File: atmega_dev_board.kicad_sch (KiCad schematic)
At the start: 44 parts, among them J1 1x15 Pin Header, J2 USB_C_Receptacle_USB2.0_16P, J3 1x15 Pin Header, J4 2x3 Pin Header, SW1 Push Button, SW2 Push Button, U1 78L05G-AB3-R, U2 HT7533-1, U3 ATmega328P-A, U4 CP2102N-Axx-xQFN28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

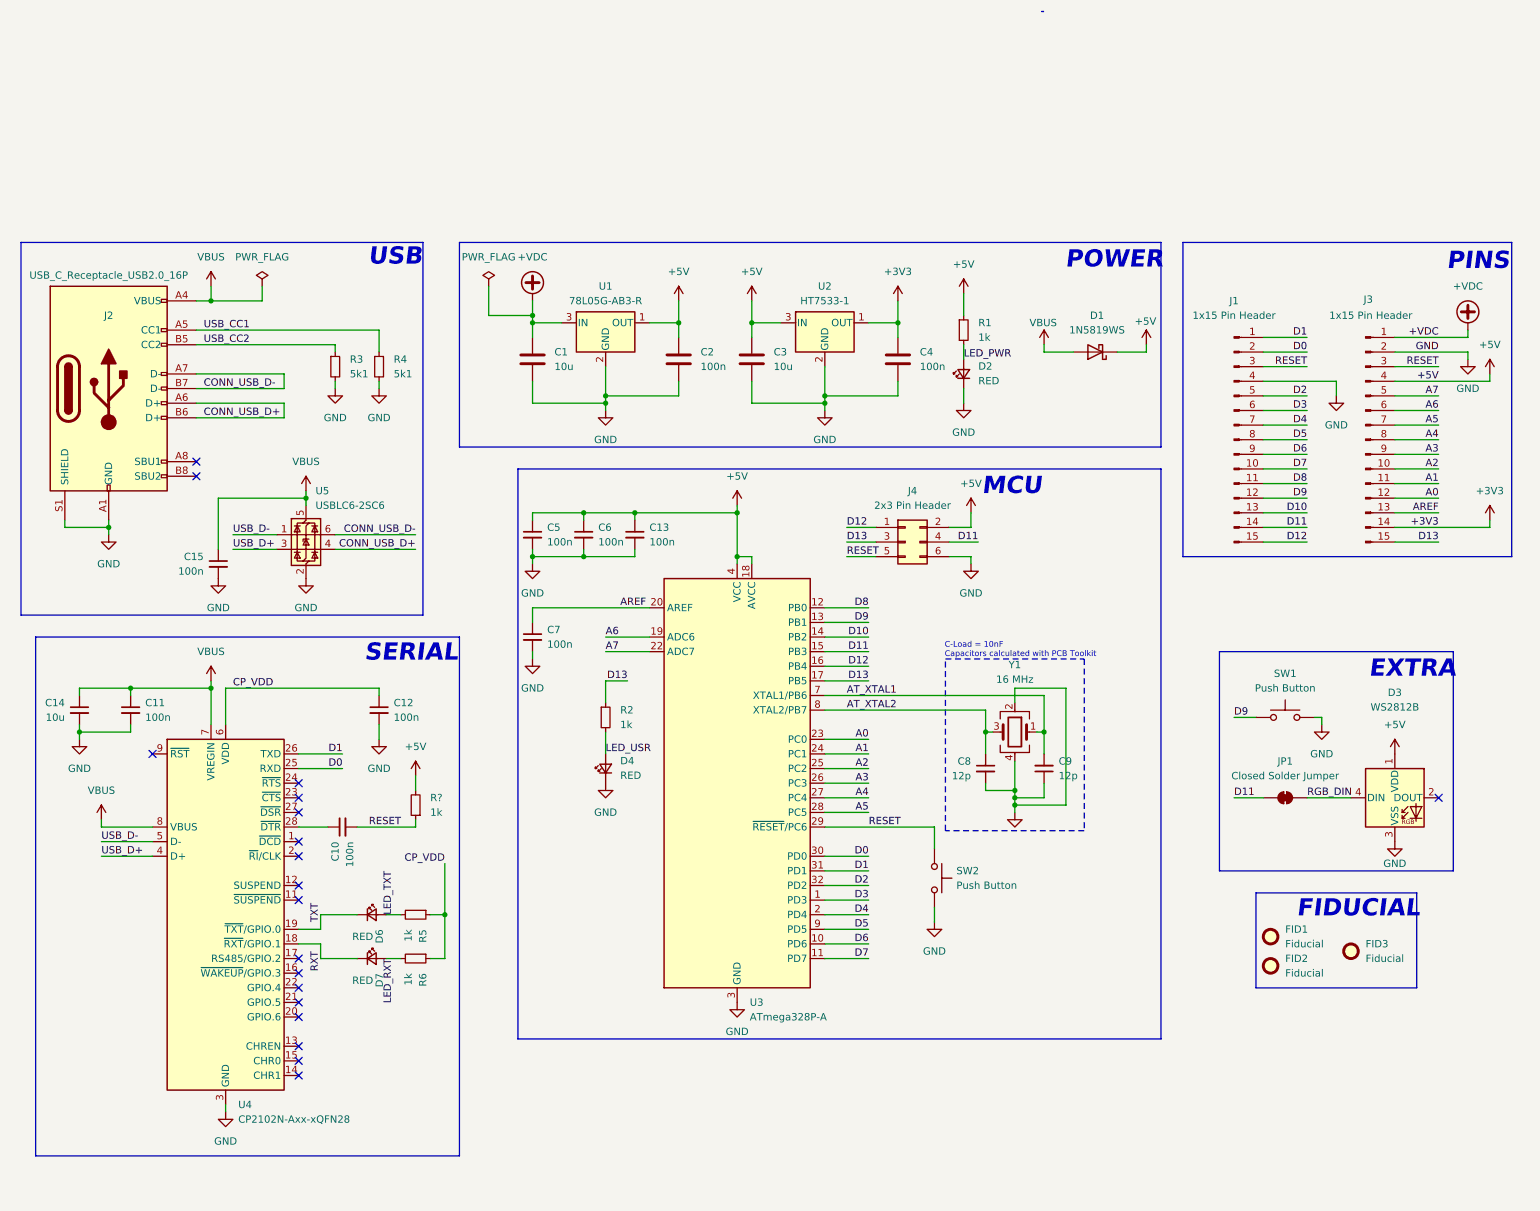
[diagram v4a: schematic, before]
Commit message: Add pull up R to RESET. Add current limiting R to USR button
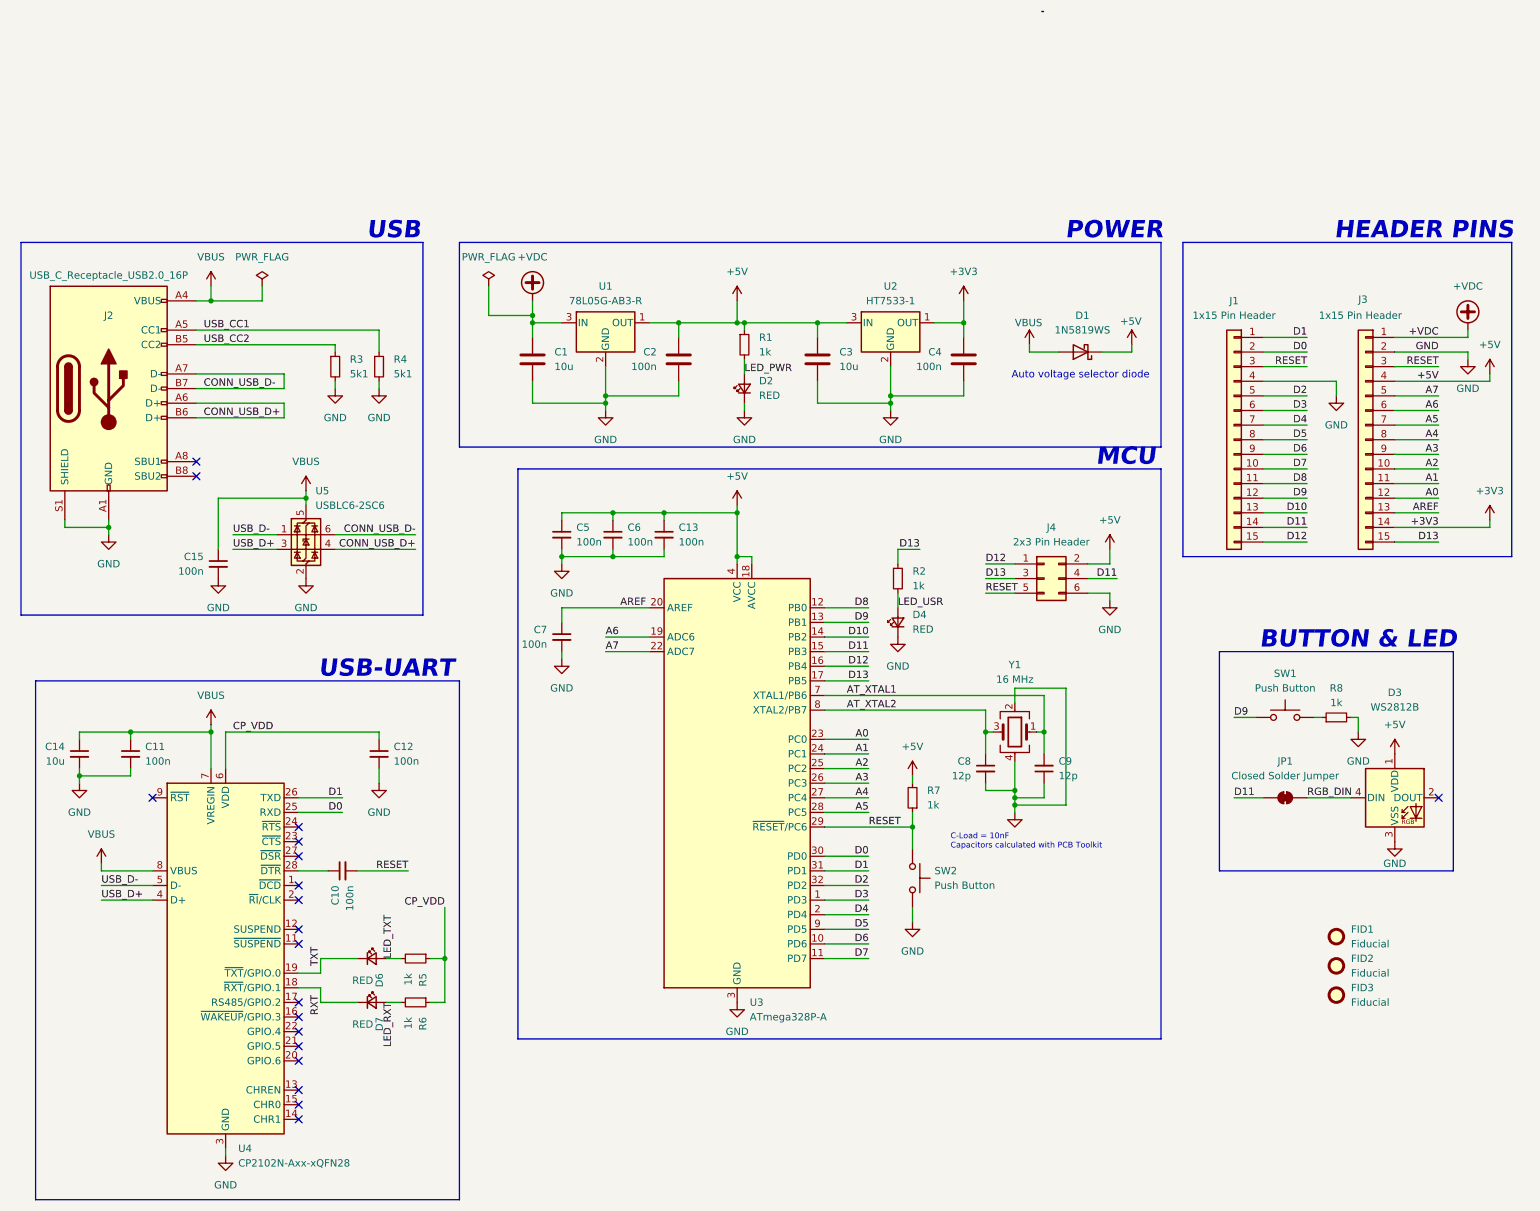
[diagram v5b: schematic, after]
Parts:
- added R8: 1k, Resistor_SMD:R_0603_1608Metric, symbol Device:R_Small
- J1, J3: symbol Connector:Conn_01x15_Pin -> Connector_Generic:Conn_01x15
- gave numbers to parts that had none: 1
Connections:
- net GND: now also R8.2; no longer SW1.2
- new net: R8.1, SW1.2
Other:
- note added: "Auto voltage selector diode"
- note added: "BUTTON & LED"
- note added: "HEADER PINS"
- note added: "USB-UART"
- note removed: "EXTRA"
- note removed: "FIDUCIAL"
- note removed: "PINS"
- note removed: "SERIAL"
- moved on the sheet: C10, C11, C12, C13, C14, C3, C4, C5, C6, C7, D1, D2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

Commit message: Finishing touches
## PCB

* Tighten zone clearance from 0.5 to 0.2
* Add silkscreen (names and logos)
* Reposition LEDs
* Round corners
* Remove unecessaary components

## SCH

* Remove extra 10 USB cap
* Remove unecessaary components

Signed-off-by: Ugo <nozolo96@gmail.com>
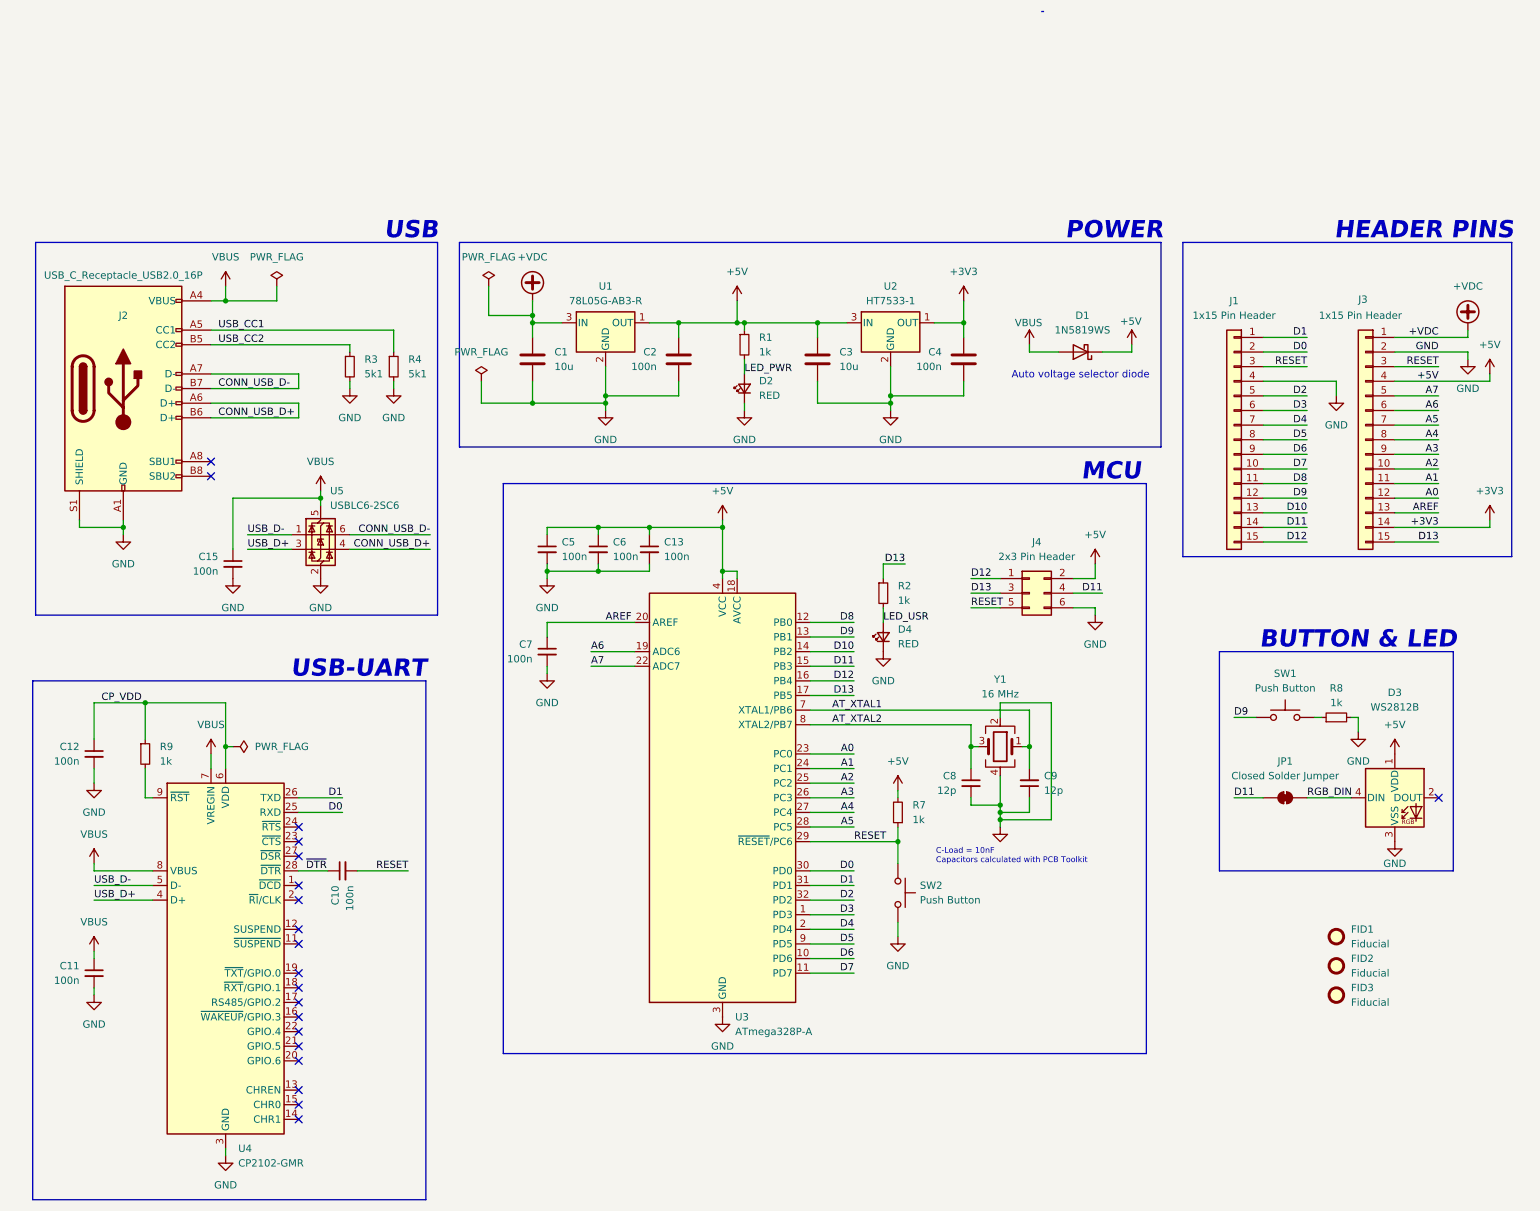
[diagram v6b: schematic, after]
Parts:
- removed C14: 10u, Capacitor_SMD:C_0603_1608Metric, symbol Device:C_Small
- removed D6, D7: RED, LED_SMD:LED_0603_1608Metric, symbol Device:LED_Small
- removed R5, R6: 1k, Resistor_SMD:R_0603_1608Metric, symbol Device:R_Small
- added R9: 1k, Resistor_SMD:R_0603_1608Metric, symbol Device:R_Small
- U4: value CP2102N-Axx-xQFN28 -> CP2102-GMR
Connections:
- net CP_VDD: now also R9.1
- net ~{DTR}: now reaches C10.1, U4.28 (~{DTR})
- net at U4.9 (~{RST}): now also R9.2
- net RXT: no longer names the net of U4.18 (~{RXT}/GPIO.1)
- net TXT: no longer names the net of U4.19 (~{TXT}/GPIO.0)
- no-connect marks 19 -> 20
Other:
- moved on the sheet: C11, C12, C13, C15, C5, C6, C7, C8, C9, D4, J2, J4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
